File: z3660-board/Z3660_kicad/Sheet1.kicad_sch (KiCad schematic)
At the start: 54 parts, among them U4 MC68060, U5 7407, X1 IQXO-70

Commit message: Update to version v0.21a
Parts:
- removed RN1: 1k, Z3660_v02:R_Array_Convex_8x0602, symbol Device:R_Pack08
- removed RN3, RN4, RN5, RN6: 22, Z3660_v02:R_Array_Convex_8x0602, symbol Device:R_Pack08
- added RN1, RN2: 1k, Z3660_v02:R_Array_Convex_4x0603, symbol Z3660_v02:R_Pack04
- added RN10, RN3, RN4, RN5, RN6, RN7, RN8, RN9: 22, Z3660_v02:R_Array_Convex_4x0603, symbol Z3660_v02:R_Pack04
- C11, C12, C13, C14, C15, C16, C17, C18, C19, C20, C21, C22, C23, C24, C25: footprint Capacitor_SMD:C_0805_2012Metric_Pad1.18x1.45mm_HandSolder -> Z3660_v02:C_0805_2012Metric_Pad1.18x1.45mm_HandSolder
- C26, C27, C28, C61, C62: footprint Capacitor_SMD:C_Elec_5x5.4 -> Z3660_v02:CP_Elec_6.3x3.9
- H1, H2, H3, H4: footprint MountingHole:MountingHole_4mm -> Z3660_v02:MountingHole_4mm
- H5, H6, H7, H8: footprint MountingHole:MountingHole_2.2mm_M2 -> Z3660_v02:MountingHole_2.2mm_M2
- JP1, JP2, JP3: footprint Connector_PinHeader_2.54mm:PinHeader_1x02_P2.54mm_Vertical -> Z3660_v02:PinHeader_1x02_P2.54mm_Vertical
- JP11, JP8: footprint Jumper:SolderJumper-3_P1.3mm_Bridged12_RoundedPad1.0x1.5mm_NumberLabels -> Z3660_v02:SolderJumper-3_P1.3mm_Bridged12_RoundedPad1.0x1.5mm_NumberLabels
- JP6, JP7: footprint Connector_PinHeader_2.54mm:PinHeader_1x03_P2.54mm_Vertical -> Z3660_v02:PinHeader_1x03_P2.54mm_Vertical
- R10, R11, R12, R19, R20, R5, R6, R7, R8, R9: footprint Resistor_SMD:R_0805_2012Metric_Pad1.20x1.40mm_HandSolder -> Z3660_v02:R_0805_2012Metric_Pad1.20x1.40mm_HandSolder
- U5: footprint Package_SO:SOIC-14_3.9x8.7mm_P1.27mm -> Z3660_v02:SOIC-14_3.9x8.7mm_P1.27mm
- U5: footprint (none) -> Z3660_v02:SOIC-14_3.9x8.7mm_P1.27mm
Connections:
- net +3V3: now also RN1.1 (R1.1), RN1.2 (R2.1)
- net 040A0: now also RN10.4 (R4.1)
- net 040A1: now also RN10.3 (R3.1)
- net 040A10: now also RN8.2 (R2.1)
- net 040A11: now also RN8.1 (R1.1)
- net 040A12: now also RN7.4 (R4.1)
- net 040A13: now also RN7.3 (R3.1)
- net 040A14: now also RN7.2 (R2.1)
- net 040A15: now also RN7.1 (R1.1)
- net 040A16: now also RN6.4 (R4.1)
- net 040A17: now also RN6.3 (R3.1)
- net 040A18: now also RN6.2 (R2.1)
- net 040A19: now also RN6.1 (R1.1)
- net 040A2: now also RN10.2 (R2.1)
- net 040A20: now also RN5.4 (R4.1)
- net 040A21: now also RN5.3 (R3.1)
- net 040A22: now also RN5.2 (R2.1)
- net 040A23: now also RN5.1 (R1.1)
- net 040A24: now also RN4.4 (R4.1)
- net 040A25: now also RN4.3 (R3.1)
- net 040A26: now also RN4.2 (R2.1)
- net 040A27: now also RN4.1 (R1.1)
- net 040A28: now also RN3.4 (R4.1)
- net 040A29: now also RN3.3 (R3.1)
- net 040A3: now also RN10.1 (R1.1)
- net 040A30: now also RN3.2 (R2.1)
- net 040A31: now also RN3.1 (R1.1)
- net 040A4: now also RN9.4 (R4.1)
- net 040A5: now also RN9.3 (R3.1)
- net 040A6: now also RN9.2 (R2.1)
- net 040A7: now also RN9.1 (R1.1)
- net 040A8: now also RN8.4 (R4.1)
- net 040A9: now also RN8.3 (R3.1)
- net 060A0: now also RN10.5 (R4.2)
- net 060A1: now also RN10.6 (R3.2)
- net 060A10: now also RN8.7 (R2.2)
- net 060A11: now also RN8.8 (R1.2)
- net 060A12: now also RN7.5 (R4.2)
- net 060A13: now also RN7.6 (R3.2)
- net 060A14: now also RN7.7 (R2.2)
- net 060A15: now also RN7.8 (R1.2)
- net 060A16: now also RN6.5 (R4.2)
- net 060A17: now also RN6.6 (R3.2)
- net 060A18: now also RN6.7 (R2.2)
- net 060A19: now also RN6.8 (R1.2)
- net 060A2: now also RN10.7 (R2.2)
- net 060A20: now also RN5.5 (R4.2)
- net 060A21: now also RN5.6 (R3.2)
- net 060A22: now also RN5.7 (R2.2)
- net 060A23: now also RN5.8 (R1.2)
- net 060A24: now also RN4.5 (R4.2)
- net 060A25: now also RN4.6 (R3.2)
- net 060A26: now also RN4.7 (R2.2)
- net 060A27: now also RN4.8 (R1.2)
- net 060A28: now also RN3.5 (R4.2)
- net 060A29: now also RN3.6 (R3.2)
- net 060A3: now also RN10.8 (R1.2)
- net 060A30: now also RN3.7 (R2.2)
- net 060A31: now also RN3.8 (R1.2)
- net 060A4: now also RN9.5 (R4.2)
- net 060A5: now also RN9.6 (R3.2)
- net 060A6: now also RN9.7 (R2.2)
- net 060A7: now also RN9.8 (R1.2)
- net 060A8: now also RN8.5 (R4.2)
- net 060A9: now also RN8.6 (R3.2)
- net Earth: now also RN1.3 (R3.1), RN1.4 (R4.1), RN2.1 (R1.1), RN2.2 (R2.1), RN2.3 (R3.1), RN2.4 (R4.1)
- net _040CIOUT: now also RN2.5 (R4.2)
- net _040EMUL: now also RN1.8 (R1.2)
- net _BGR040: now also RN2.7 (R2.2)
- net _TBI: now also RN1.7 (R2.2)
- net at U4.147 (TDI): now also RN2.6 (R3.2)
- net at U4.164 (~{TRST}): now also RN2.8 (R1.2)
- net at U4.148 (TCK): now also RN1.5 (R4.2)
- net at U4.149 (TMS): now also RN1.6 (R3.2)

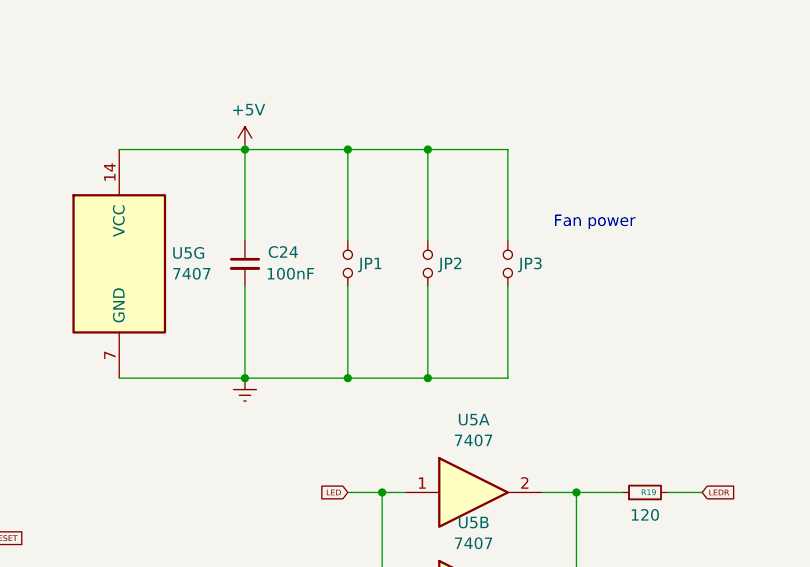
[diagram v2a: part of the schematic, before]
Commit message: Update to PCB v0.21d Minor change in footprint of fans
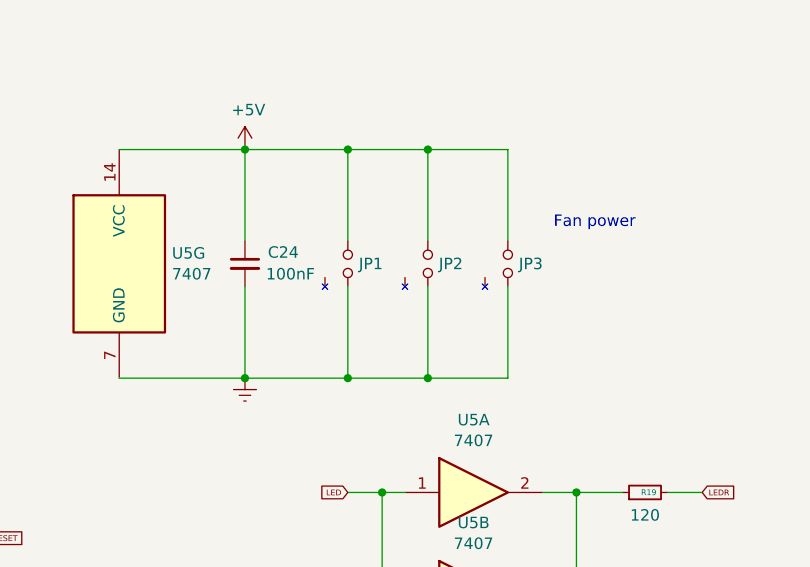
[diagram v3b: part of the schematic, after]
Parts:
- JP1: footprint Z3660_v02:PinHeader_1x02_P2.54mm_Vertical -> Z3660_v02:PinHeader_1x03_P2.54mm_Horizontal
- JP2: footprint Z3660_v02:PinHeader_1x02_P2.54mm_Vertical -> Z3660_v02:PinHeader_1x03_P2.54mm_Vertical; symbol Device:Jumper_NO_Small -> Z3660_v02:Jumper_NO_Small_1
- JP3: footprint Z3660_v02:PinHeader_1x02_P2.54mm_Vertical -> Z3660_v02:PinHeader_1x03_P2.54mm_Horizontal; symbol Device:Jumper_NO_Small -> Z3660_v02:Jumper_NO_Small_1
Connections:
- net +5V: now also JP1.2, JP2.2, JP3.2; no longer JP1.1, JP2.1, JP3.1
- net Earth: now also JP1.1, JP2.1, JP3.1; no longer JP1.2, JP2.2, JP3.2
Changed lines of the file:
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@@
   (title_block
     (title "Z3660 by sHaNsHe (Double H Tech)")
-    (date "2024-02-09")
-    (rev "v0.21b")
+    (date "2024-03-03")
+    (rev "v0.21d")
     (comment 1 "v0.21a Changed Array Networks")
     (comment 2 "v0.21b Changed the 060 socket")
+    (comment 3 "v0.21c wrongly named")
+    (comment 4 "v0.21d Changed fan header to right angle")
   )
   (junction (at 129.54 46.99) (diameter 0) (color 0 0 0 0)
@@
     )
   )
-  (symbol (lib_id "Device:Jumper_NO_Small") (at 340.36 71.12 270) (unit 1)
+  (symbol (lib_id "Z3660_v02:Jumper_NO_Small_1") (at 340.36 71.12 270) (mirror x) (unit 1)
     (in_bom yes) (on_board yes) (dnp no)
     (property "Reference" "JP2" (at 341.5792 71.12 90)
       (effects (font (size 1.27 1.27)) (justify left))
     )
-    (property "Value" "Jumper_NO_Small" (at 341.5792 72.263 90)
+    (property "Value" "Jumper_NO_Small" (at 341.5792 69.977 90)
       (effects (font (size 1.27 1.27)) (justify left) hide)
     )
-    (property "Footprint" "Z3660_v02:PinHeader_1x02_P2.54mm_Vertical" (at 340.36 71.12 0)
+    (property "Footprint" "Z3660_v02:PinHeader_1x03_P2.54mm_Vertical" (at 335.28 69.85 0)
       (effects (font (size 1.27 1.27)) hide)
     )
@@
     (pin "1")
     (pin "2")
+    (pin "3")
     (instances
       (project "Z3660_v021b"
@@
     )
   )
-  (symbol (lib_id "Device:Jumper_NO_Small") (at 331.47 71.12 270) (unit 1)
+  (symbol (lib_name "Jumper_NO_Small_1") (lib_id "Device:Jumper_NO_Small") (at 331.47 71.12 270) (mirror x) (unit 1)
     (in_bom yes) (on_board yes) (dnp no)
     (property "Reference" "JP1" (at 332.6892 71.12 90)
       (effects (font (size 1.27 1.27)) (justify left))
     )
-    (property "Value" "Jumper_NO_Small" (at 332.6892 72.263 90)
+    (property "Value" "Jumper_NO_Small" (at 332.6892 69.977 90)
       (effects (font (size 1.27 1.27)) (justify left) hide)
     )
-    (property "Footprint" "Z3660_v02:PinHeader_1x02_P2.54mm_Vertical" (at 331.47 71.12 0)
+    (property "Footprint" "Z3660_v02:PinHeader_1x03_P2.54mm_Horizontal" (at 326.39 69.85 0)
       (effects (font (size 1.27 1.27)) hide)
     )
@@
     (pin "1")
     (pin "2")
+    (pin "3")
     (instances
       (project "Z3660_v021b"
@@
     )
   )
-  (symbol (lib_id "Device:Jumper_NO_Small") (at 349.25 71.12 270) (unit 1)
+  (symbol (lib_id "Z3660_v02:Jumper_NO_Small_1") (at 349.25 71.12 270) (mirror x) (unit 1)
     (in_bom yes) (on_board yes) (dnp no)
     (property "Reference" "JP3" (at 350.4692 71.12 90)
       (effects (font (size 1.27 1.27)) (justify left))
     )
-    (property "Value" "Jumper_NO_Small" (at 350.4692 72.263 90)
+    (property "Value" "Jumper_NO_Small" (at 350.4692 69.977 90)
       (effects (font (size 1.27 1.27)) (justify left) hide)
     )
-    (property "Footprint" "Z3660_v02:PinHeader_1x02_P2.54mm_Vertical" (at 349.25 71.12 0)
+    (property "Footprint" "Z3660_v02:PinHeader_1x03_P2.54mm_Horizontal" (at 344.17 69.85 0)
       (effects (font (size 1.27 1.27)) hide)
     )
@@
     (pin "1")
     (pin "2")
+    (pin "3")
     (instances
       (project "Z3660_v021b"
